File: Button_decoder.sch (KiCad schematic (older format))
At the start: 18 parts

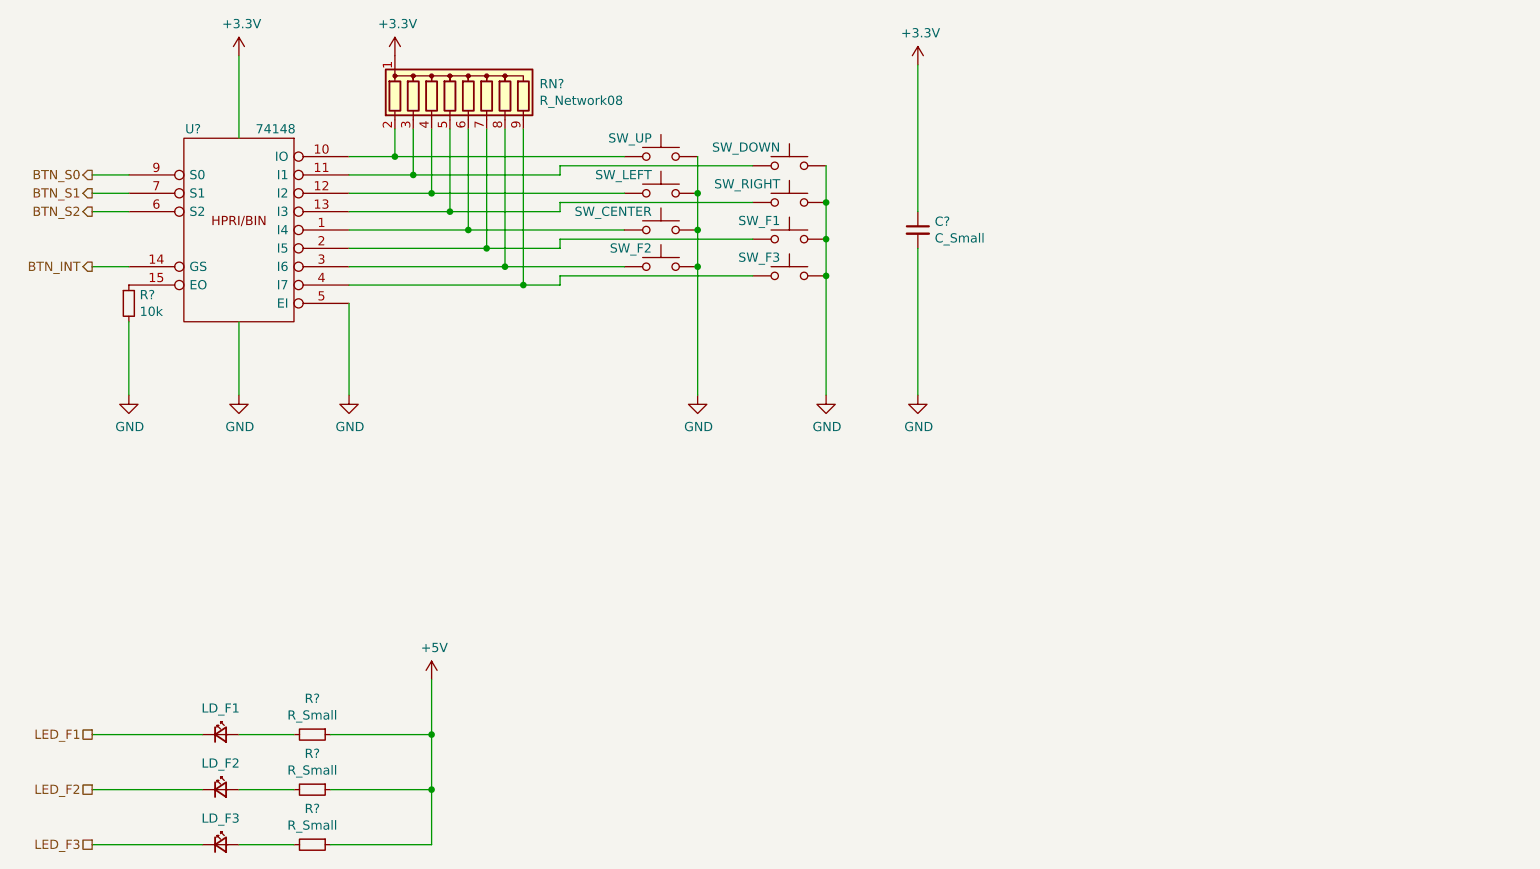
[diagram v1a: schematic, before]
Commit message: Bauteile grob platziert
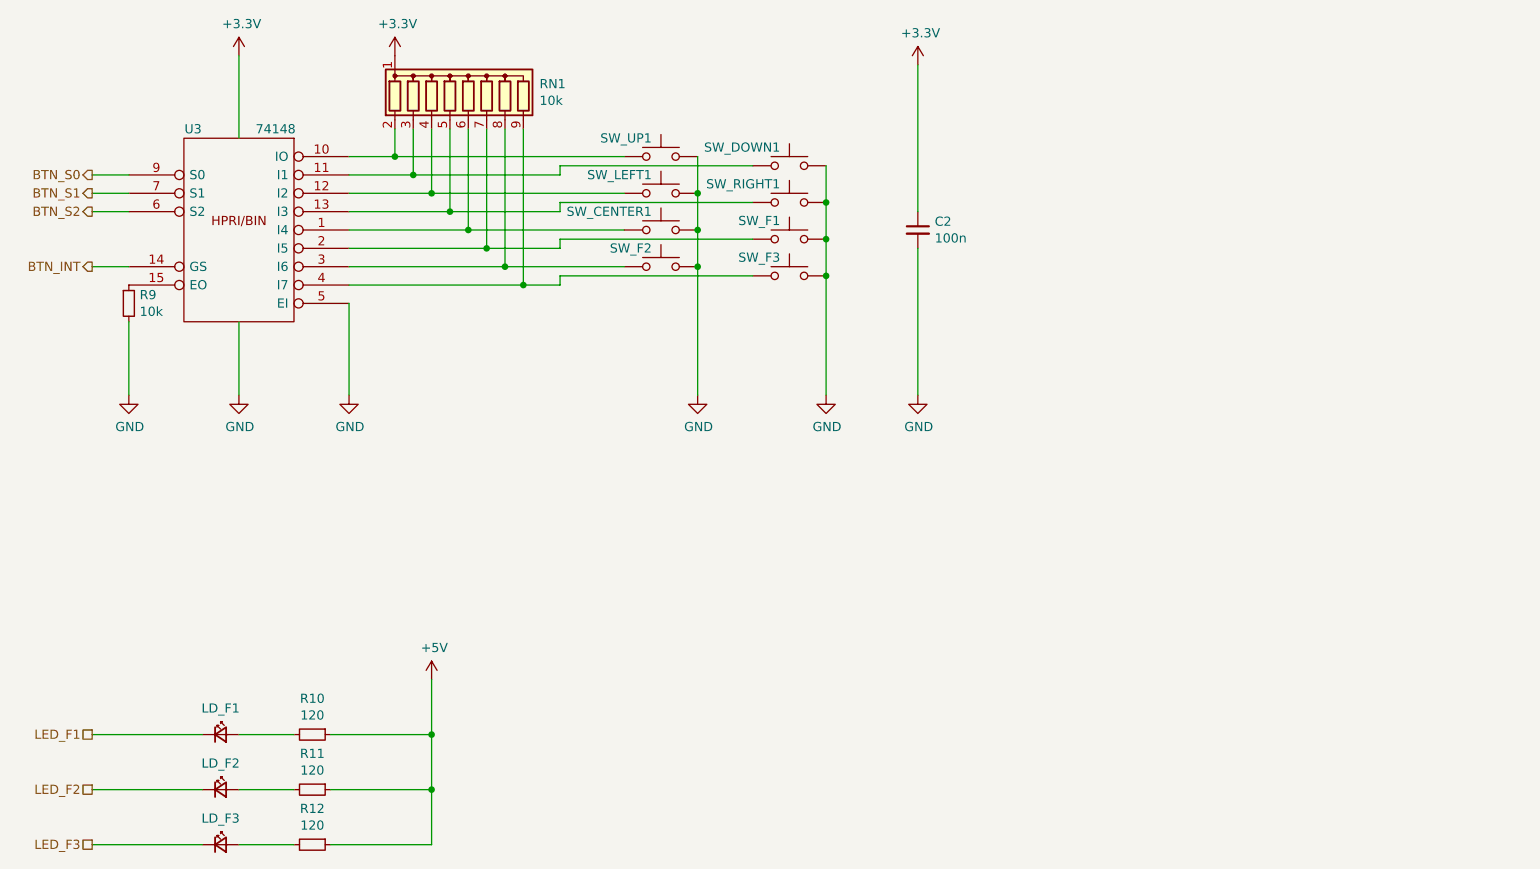
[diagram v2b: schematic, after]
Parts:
- C2: renamed from C?; value C_Small -> 100n; footprint (none) -> Capacitor_SMD:C_0603_1608Metric_Pad1.05x0.95mm_HandSolder
- LD_F1, LD_F2, LD_F3: footprint (none) -> LED_THT:LED_D3.0mm
- R10, R11, R12: renamed from R?; value R_Small -> 120; footprint (none) -> Resistor_SMD:R_0603_1608Metric_Pad1.05x0.95mm_HandSolder
- R9: renamed from R?; footprint (none) -> Resistor_SMD:R_0603_1608Metric_Pad1.05x0.95mm_HandSolder
- RN1: renamed from RN?; value R_Network08 -> 10k
- SW_CENTER1: renamed from SW_CENTER; footprint (none) -> Button_Switch_SMD:SW_MEC_5GSH9
- SW_DOWN1: renamed from SW_DOWN; footprint (none) -> Button_Switch_SMD:SW_MEC_5GSH9
- SW_F1, SW_F2, SW_F3: footprint (none) -> Button_Switch_SMD:SW_MEC_5GSH9
- SW_LEFT1: renamed from SW_LEFT; footprint (none) -> Button_Switch_SMD:SW_MEC_5GSH9
- SW_RIGHT1: renamed from SW_RIGHT; footprint (none) -> Button_Switch_SMD:SW_MEC_5GSH9
- SW_UP1: renamed from SW_UP; footprint (none) -> Button_Switch_SMD:SW_MEC_5GSH9
- U3: renamed from U?; footprint (none) -> Package_SO:SOIC-16_3.9x9.9mm_P1.27mm
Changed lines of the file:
@@
 BTN_INT
 $Comp
-L 74xx_IEEE:74148 U?
+L 74xx_IEEE:74148 U3
 U 1 1 5EFADAFE
 P 3300 2750
-F 0 "U?" H 3550 3300 50  0000 C CNN
+F 0 "U3" H 3550 3300 50  0000 C CNN
 F 1 "74148" H 3100 3300 50  0000 C CNN
-F 2 "" H 3300 2750 50  0001 C CNN
+F 2 "Package_SO:SOIC-16_3.9x9.9mm_P1.27mm" H 3300 2750 50  0001 C CNN
 F 3 "" H 3300 2750 50  0001 C CNN
 	1    3300 2750
@@
 	2500 2950 2700 2950
 $Comp
-L power:+3.3V #PWR?
+L power:+3.3V #PWR0110
 U 1 1 5EFAFAAB
 P 3300 1800
-F 0 "#PWR?" H 3300 1650 50  0001 C CNN
+F 0 "#PWR0110" H 3300 1650 50  0001 C CNN
 F 1 "+3.3V" H 3315 1973 50  0000 C CNN
 F 2 "" H 3300 1800 50  0001 C CNN
@@
 	3300 1800 3300 2250
 $Comp
-L power:GND #PWR?
+L power:GND #PWR0111
 U 1 1 5EFAFEDD
 P 3300 3650
-F 0 "#PWR?" H 3300 3400 50  0001 C CNN
+F 0 "#PWR0111" H 3300 3400 50  0001 C CNN
 F 1 "GND" H 3305 3477 50  0000 C CNN
 F 2 "" H 3300 3650 50  0001 C CNN
@@
 	3300 3650 3300 3250
 $Comp
-L power:GND #PWR?
+L power:GND #PWR0112
 U 1 1 5EFB0576
 P 2700 3650
-F 0 "#PWR?" H 2700 3400 50  0001 C CNN
+F 0 "#PWR0112" H 2700 3400 50  0001 C CNN
 F 1 "GND" H 2705 3477 50  0000 C CNN
 F 2 "" H 2700 3650 50  0001 C CNN
@@
 $EndComp
 $Comp
-L Device:R_Small R?
+L Device:R_Small R9
 U 1 1 5EFB06F4
 P 2700 3150
-F 0 "R?" H 2759 3196 50  0000 L CNN
+F 0 "R9" H 2759 3196 50  0000 L CNN
 F 1 "10k" H 2759 3105 50  0000 L CNN
-F 2 "" H 2700 3150 50  0001 C CNN
+F 2 "Resistor_SMD:R_0603_1608Metric_Pad1.05x0.95mm_HandSolder" H 2700 3150 50  0001 C CNN
 F 3 "~" H 2700 3150 50  0001 C CNN
 	1    2700 3150
@@
 	2700 3250 2700 3650
 $Comp
-L Device:R_Network08 RN?
+L Device:R_Network08 RN1
 U 1 1 5EFB12E3
 P 4550 2000
-F 0 "RN?" H 4938 2046 50  0000 L CNN
-F 1 "R_Network08" H 4938 1955 50  0000 L CNN
+F 0 "RN1" H 4938 2046 50  0000 L CNN
+F 1 "10k" H 4938 1955 50  0000 L CNN
 F 2 "Resistor_THT:R_Array_SIP9" V 5025 2000 50  0001 C CNN
 F 3 "http://www.vishay.com/docs/31509/csc.pdf" H 4550 2000 50  0001 C CNN
@@
 $EndComp
 $Comp
-L power:+3.3V #PWR?
+L power:+3.3V #PWR0113
 U 1 1 5EFB2E2E
 P 4150 1800
-F 0 "#PWR?" H 4150 1650 50  0001 C CNN
+F 0 "#PWR0113" H 4150 1650 50  0001 C CNN
 F 1 "+3.3V" H 4165 1973 50  0000 C CNN
 F 2 "" H 4150 1800 50  0001 C CNN
@@
 $EndComp
 $Comp
-L Switch:SW_MEC_5G SW_UP
+L Switch:SW_MEC_5G SW_UP1
 U 1 1 5EFB42CA
 P 5600 2350
-F 0 "SW_UP" H 5550 2450 50  0000 R CNN
+F 0 "SW_UP1" H 5550 2450 50  0000 R CNN
 F 1 "SW_MEC_5G" H 5850 2450 50  0001 C CNN
-F 2 "" H 5600 2550 50  0001 C CNN
+F 2 "Button_Switch_SMD:SW_MEC_5GSH9" H 5600 2550 50  0001 C CNN
 F 3 "http://www.apem.com/int/index.php?controller=attachment&id_attachment=488" H 5600 2550 50  0001 C CNN
 	1    5600 2350
@@
 	4850 3050 3900 3050
 $Comp
-L Switch:SW_MEC_5G SW_LEFT
+L Switch:SW_MEC_5G SW_LEFT1
 U 1 1 5EFE1803
 P 5600 2550
-F 0 "SW_LEFT" H 5550 2650 50  0000 R CNN
+F 0 "SW_LEFT1" H 5550 2650 50  0000 R CNN
 F 1 "SW_MEC_5G" H 5850 2650 50  0001 C CNN
-F 2 "" H 5600 2750 50  0001 C CNN
+F 2 "Button_Switch_SMD:SW_MEC_5GSH9" H 5600 2750 50  0001 C CNN
 F 3 "http://www.apem.com/int/index.php?controller=attachment&id_attachment=488" H 5600 2750 50  0001 C CNN
 	1    5600 2550
@@
 $EndComp
 $Comp
-L Switch:SW_MEC_5G SW_CENTER
+L Switch:SW_MEC_5G SW_CENTER1
 U 1 1 5EFE1FDD
 P 5600 2750
-F 0 "SW_CENTER" H 5550 2850 50  0000 R CNN
+F 0 "SW_CENTER1" H 5550 2850 50  0000 R CNN
 F 1 "SW_MEC_5G" H 5850 2850 50  0001 C CNN
-F 2 "" H 5600 2950 50  0001 C CNN
+F 2 "Button_Switch_SMD:SW_MEC_5GSH9" H 5600 2950 50  0001 C CNN
 F 3 "http://www.apem.com/int/index.php?controller=attachment&id_attachment=488" H 5600 2950 50  0001 C CNN
 	1    5600 2750
@@
 F 0 "SW_F2" H 5550 3050 50  0000 R CNN
 F 1 "SW_MEC_5G" H 5850 3050 50  0001 C CNN
-F 2 "" H 5600 3150 50  0001 C CNN
+F 2 "Button_Switch_SMD:SW_MEC_5GSH9" H 5600 3150 50  0001 C CNN
 F 3 "http://www.apem.com/int/index.php?controller=attachment&id_attachment=488" H 5600 3150 50  0001 C CNN
 	1    5600 2950
@@
 $EndComp
 $Comp
-L Switch:SW_MEC_5G SW_DOWN
+L Switch:SW_MEC_5G SW_DOWN1
 U 1 1 5EFF38EE
 P 6300 2400
-F 0 "SW_DOWN" H 6250 2500 50  0000 R CNN
+F 0 "SW_DOWN1" H 6250 2500 50  0000 R CNN
 F 1 "SW_MEC_5G" H 6550 2500 50  0001 C CNN
-F 2 "" H 6300 2600 50  0001 C CNN
+F 2 "Button_Switch_SMD:SW_MEC_5GSH9" H 6300 2600 50  0001 C CNN
 F 3 "http://www.apem.com/int/index.php?controller=attachment&id_attachment=488" H 6300 2600 50  0001 C CNN
 	1    6300 2400
@@
 $EndComp
 $Comp
-L Switch:SW_MEC_5G SW_RIGHT
+L Switch:SW_MEC_5G SW_RIGHT1
 U 1 1 5EFF3FB1
 P 6300 2600
-F 0 "SW_RIGHT" H 6250 2700 50  0000 R CNN
+F 0 "SW_RIGHT1" H 6250 2700 50  0000 R CNN
 F 1 "SW_MEC_5G" H 6550 2700 50  0001 C CNN
-F 2 "" H 6300 2800 50  0001 C CNN
+F 2 "Button_Switch_SMD:SW_MEC_5GSH9" H 6300 2800 50  0001 C CNN
 F 3 "http://www.apem.com/int/index.php?controller=attachment&id_attachment=488" H 6300 2800 50  0001 C CNN
 	1    6300 2600
@@
 F 0 "SW_F1" H 6250 2900 50  0000 R CNN
 F 1 "SW_MEC_5G" H 6550 2900 50  0001 C CNN
-F 2 "" H 6300 3000 50  0001 C CNN
+F 2 "Button_Switch_SMD:SW_MEC_5GSH9" H 6300 3000 50  0001 C CNN
 F 3 "http://www.apem.com/int/index.php?controller=attachment&id_attachment=488" H 6300 3000 50  0001 C CNN
 	1    6300 2800
@@
 F 0 "SW_F3" H 6250 3100 50  0000 R CNN
 F 1 "SW_MEC_5G" H 6550 3100 50  0001 C CNN
-F 2 "" H 6300 3200 50  0001 C CNN
+F 2 "Button_Switch_SMD:SW_MEC_5GSH9" H 6300 3200 50  0001 C CNN
 F 3 "http://www.apem.com/int/index.php?controller=attachment&id_attachment=488" H 6300 3200 50  0001 C CNN
 	1    6300 3000
@@
 $EndComp
 $Comp
-L power:GND #PWR?
+L power:GND #PWR0114
 U 1 1 5F000955
 P 5800 3650
-F 0 "#PWR?" H 5800 3400 50  0001 C CNN
+F 0 "#PWR0114" H 5800 3400 50  0001 C CNN
 F 1 "GND" H 5805 3477 50  0000 C CNN
 F 2 "" H 5800 3650 50  0001 C CNN
@@
 $EndComp
 $Comp
-L power:GND #PWR?
+L power:GND #PWR0115
 U 1 1 5F00123E
 P 6500 3650
-F 0 "#PWR?" H 6500 3400 50  0001 C CNN
+F 0 "#PWR0115" H 6500 3400 50  0001 C CNN
 F 1 "GND" H 6505 3477 50  0000 C CNN
 F 2 "" H 6500 3650 50  0001 C CNN
@@
 	6500 3000 6500 3650
 $Comp
-L power:GND #PWR?
+L power:GND #PWR0116
 U 1 1 5F008E80
 P 3900 3650
-F 0 "#PWR?" H 3900 3400 50  0001 C CNN
+F 0 "#PWR0116" H 3900 3400 50  0001 C CNN
 F 1 "GND" H 3905 3477 50  0000 C CNN
 F 2 "" H 3900 3650 50  0001 C CNN
@@
 	3900 3650 3900 3150
 $Comp
-L power:GND #PWR?
+L power:GND #PWR0117
 U 1 1 5F00A4A8
 P 7000 3650
-F 0 "#PWR?" H 7000 3400 50  0001 C CNN
+F 0 "#PWR0117" H 7000 3400 50  0001 C CNN
 F 1 "GND" H 7005 3477 50  0000 C CNN
 F 2 "" H 7000 3650 50  0001 C CNN
@@
 $EndComp
 $Comp
-L power:+3.3V #PWR?
+L power:+3.3V #PWR0118
 U 1 1 5F00BBF0
 P 7000 1850
-F 0 "#PWR?" H 7000 1700 50  0001 C CNN
+F 0 "#PWR0118" H 7000 1700 50  0001 C CNN
 F 1 "+3.3V" H 7015 2023 50  0000 C CNN
 F 2 "" H 7000 1850 50  0001 C CNN
@@
 $EndComp
 $Comp
-L Device:C_Small C?
+L Device:C_Small C2
 U 1 1 5F00C881
 P 7000 2750
-F 0 "C?" H 7092 2796 50  0000 L CNN
-F 1 "C_Small" H 7092 2705 50  0000 L CNN
-F 2 "" H 7000 2750 50  0001 C CNN
+F 0 "C2" H 7092 2796 50  0000 L CNN
+F 1 "100n" H 7092 2705 50  0000 L CNN
+F 2 "Capacitor_SMD:C_0603_1608Metric_Pad1.05x0.95mm_HandSolder" H 7000 2750 50  0001 C CNN
 F 3 "~" H 7000 2750 50  0001 C CNN
 	1    7000 2750
@@
 	7000 2850 7000 3650
 $Comp
-L Device:R_Small R?
+L Device:R_Small R10
 U 1 1 5F00F388
 P 3700 5500
-F 0 "R?" V 3504 5500 50  0000 C CNN
-F 1 "R_Small" V 3595 5500 50  0000 C CNN
-F 2 "" H 3700 5500 50  0001 C CNN
+F 0 "R10" V 3504 5500 50  0000 C CNN
+F 1 "120" V 3595 5500 50  0000 C CNN
+F 2 "Resistor_SMD:R_0603_1608Metric_Pad1.05x0.95mm_HandSolder" H 3700 5500 50  0001 C CNN
 F 3 "~" H 3700 5500 50  0001 C CNN
 	1    3700 5500
@@
 F 0 "LD_F1" H 3200 5643 50  0000 C CNN
 F 1 "LED_Small" H 3200 5644 50  0001 C CNN
-F 2 "" V 3200 5500 50  0001 C CNN
+F 2 "LED_THT:LED_D3.0mm" V 3200 5500 50  0001 C CNN
 F 3 "~" V 3200 5500 50  0001 C CNN
 	1    3200 5500
@@
 	3300 5500 3600 5500
 $Comp
-L Device:R_Small R?
+L Device:R_Small R11
 U 1 1 5F011E08
 P 3700 5800
-F 0 "R?" V 3504 5800 50  0000 C CNN
-F 1 "R_Small" V 3595 5800 50  0000 C CNN
-F 2 "" H 3700 5800 50  0001 C CNN
+F 0 "R11" V 3504 5800 50  0000 C CNN
+F 1 "120" V 3595 5800 50  0000 C CNN
+F 2 "Resistor_SMD:R_0603_1608Metric_Pad1.05x0.95mm_HandSolder" H 3700 5800 50  0001 C CNN
 F 3 "~" H 3700 5800 50  0001 C CNN
 	1    3700 5800
@@
 F 0 "LD_F2" H 3200 5943 50  0000 C CNN
 F 1 "LED_Small" H 3200 5944 50  0001 C CNN
-F 2 "" V 3200 5800 50  0001 C CNN
+F 2 "LED_THT:LED_D3.0mm" V 3200 5800 50  0001 C CNN
 F 3 "~" V 3200 5800 50  0001 C CNN
 	1    3200 5800
@@
 	3300 5800 3600 5800
 $Comp
-L Device:R_Small R?
+L Device:R_Small R12
 U 1 1 5F01298E
 P 3700 6100
-F 0 "R?" V 3504 6100 50  0000 C CNN
-F 1 "R_Small" V 3595 6100 50  0000 C CNN
-F 2 "" H 3700 6100 50  0001 C CNN
+F 0 "R12" V 3504 6100 50  0000 C CNN
+F 1 "120" V 3595 6100 50  0000 C CNN
+F 2 "Resistor_SMD:R_0603_1608Metric_Pad1.05x0.95mm_HandSolder" H 3700 6100 50  0001 C CNN
 F 3 "~" H 3700 6100 50  0001 C CNN
 	1    3700 6100
@@
 F 0 "LD_F3" H 3200 6243 50  0000 C CNN
 F 1 "LED_Small" H 3200 6244 50  0001 C CNN
-F 2 "" V 3200 6100 50  0001 C CNN
+F 2 "LED_THT:LED_D3.0mm" V 3200 6100 50  0001 C CNN
 F 3 "~" V 3200 6100 50  0001 C CNN
 	1    3200 6100
@@
 	3300 6100 3600 6100
 $Comp
-L power:+5V #PWR?
+L power:+5V #PWR0119
 U 1 1 5F01432E
 P 4350 5200
-F 0 "#PWR?" H 4350 5050 50  0001 C CNN
+F 0 "#PWR0119" H 4350 5050 50  0001 C CNN
 F 1 "+5V" H 4365 5373 50  0000 C CNN
 F 2 "" H 4350 5200 50  0001 C CNN

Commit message: Alle Bauteile platziert
Alle Bauteile sind grob plaziert.
Einige Bauteile sollten noch umplaziert werden (u. a. die Jumper links neben Groov-Con, RGB-LED,).
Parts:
- C2: symbol Device:C_Small -> MCT_Labor_5529-rescue:C_Small-Device
- LD_F1, LD_F2, LD_F3: symbol Device:LED_Small -> MCT_Labor_5529-rescue:LED_Small-Device
- R10, R11, R12, R9: symbol Device:R_Small -> MCT_Labor_5529-rescue:R_Small-Device
- RN1: symbol Device:R_Network08 -> MCT_Labor_5529-rescue:R_Network08-Device
- SW_CENTER1, SW_DOWN1, SW_F1, SW_F2, SW_F3, SW_LEFT1, SW_RIGHT1, SW_UP1: symbol Switch:SW_MEC_5G -> MCT_Labor_5529-rescue:SW_MEC_5G-Switch
- U3: symbol 74xx_IEEE:74148 -> MCT_Labor_5529-rescue:74148-74xx_IEEE
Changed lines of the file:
@@
 BTN_INT
 $Comp
-L 74xx_IEEE:74148 U3
+L MCT_Labor_5529-rescue:74148-74xx_IEEE U3
 U 1 1 5EFADAFE
 P 3300 2750
@@
 	2500 2950 2700 2950
 $Comp
-L power:+3.3V #PWR0110
+L MCT_Labor_5529-rescue:+3.3V-power #PWR0110
 U 1 1 5EFAFAAB
 P 3300 1800
@@
 	3300 1800 3300 2250
 $Comp
-L power:GND #PWR0111
+L MCT_Labor_5529-rescue:GND-power #PWR0111
 U 1 1 5EFAFEDD
 P 3300 3650
@@
 	3300 3650 3300 3250
 $Comp
-L power:GND #PWR0112
+L MCT_Labor_5529-rescue:GND-power #PWR0112
 U 1 1 5EFB0576
 P 2700 3650
@@
 $EndComp
 $Comp
-L Device:R_Small R9
+L MCT_Labor_5529-rescue:R_Small-Device R9
 U 1 1 5EFB06F4
 P 2700 3150
@@
 	2700 3250 2700 3650
 $Comp
-L Device:R_Network08 RN1
+L MCT_Labor_5529-rescue:R_Network08-Device RN1
 U 1 1 5EFB12E3
 P 4550 2000
@@
 $EndComp
 $Comp
-L power:+3.3V #PWR0113
+L MCT_Labor_5529-rescue:+3.3V-power #PWR0113
 U 1 1 5EFB2E2E
 P 4150 1800
@@
 $EndComp
 $Comp
-L Switch:SW_MEC_5G SW_UP1
+L MCT_Labor_5529-rescue:SW_MEC_5G-Switch SW_UP1
 U 1 1 5EFB42CA
 P 5600 2350
@@
 	4850 3050 3900 3050
 $Comp
-L Switch:SW_MEC_5G SW_LEFT1
+L MCT_Labor_5529-rescue:SW_MEC_5G-Switch SW_LEFT1
 U 1 1 5EFE1803
 P 5600 2550
@@
 $EndComp
 $Comp
-L Switch:SW_MEC_5G SW_CENTER1
+L MCT_Labor_5529-rescue:SW_MEC_5G-Switch SW_CENTER1
 U 1 1 5EFE1FDD
 P 5600 2750
@@
 $EndComp
 $Comp
-L Switch:SW_MEC_5G SW_F2
+L MCT_Labor_5529-rescue:SW_MEC_5G-Switch SW_F2
 U 1 1 5EFE26F5
 P 5600 2950
@@
 $EndComp
 $Comp
-L Switch:SW_MEC_5G SW_DOWN1
+L MCT_Labor_5529-rescue:SW_MEC_5G-Switch SW_DOWN1
 U 1 1 5EFF38EE
 P 6300 2400
@@
 $EndComp
 $Comp
-L Switch:SW_MEC_5G SW_RIGHT1
+L MCT_Labor_5529-rescue:SW_MEC_5G-Switch SW_RIGHT1
 U 1 1 5EFF3FB1
 P 6300 2600
@@
 $EndComp
 $Comp
-L Switch:SW_MEC_5G SW_F1
+L MCT_Labor_5529-rescue:SW_MEC_5G-Switch SW_F1
 U 1 1 5EFF483B
 P 6300 2800
@@
 $EndComp
 $Comp
-L Switch:SW_MEC_5G SW_F3
+L MCT_Labor_5529-rescue:SW_MEC_5G-Switch SW_F3
 U 1 1 5EFF4FB0
 P 6300 3000
@@
 $EndComp
 $Comp
-L power:GND #PWR0114
+L MCT_Labor_5529-rescue:GND-power #PWR0114
 U 1 1 5F000955
 P 5800 3650
@@
 $EndComp
 $Comp
-L power:GND #PWR0115
+L MCT_Labor_5529-rescue:GND-power #PWR0115
 U 1 1 5F00123E
 P 6500 3650
@@
 	6500 3000 6500 3650
 $Comp
-L power:GND #PWR0116
+L MCT_Labor_5529-rescue:GND-power #PWR0116
 U 1 1 5F008E80
 P 3900 3650
@@
 	3900 3650 3900 3150
 $Comp
-L power:GND #PWR0117
+L MCT_Labor_5529-rescue:GND-power #PWR0117
 U 1 1 5F00A4A8
 P 7000 3650
@@
 $EndComp
 $Comp
-L power:+3.3V #PWR0118
+L MCT_Labor_5529-rescue:+3.3V-power #PWR0118
 U 1 1 5F00BBF0
 P 7000 1850
@@
 $EndComp
 $Comp
-L Device:C_Small C2
+L MCT_Labor_5529-rescue:C_Small-Device C2
 U 1 1 5F00C881
 P 7000 2750
@@
 	7000 2850 7000 3650
 $Comp
-L Device:R_Small R10
+L MCT_Labor_5529-rescue:R_Small-Device R10
 U 1 1 5F00F388
 P 3700 5500
@@
 $EndComp
 $Comp
-L Device:LED_Small LD_F1
+L MCT_Labor_5529-rescue:LED_Small-Device LD_F1
 U 1 1 5F00FA81
 P 3200 5500
@@
 	3300 5500 3600 5500
 $Comp
-L Device:R_Small R11
+L MCT_Labor_5529-rescue:R_Small-Device R11
 U 1 1 5F011E08
 P 3700 5800
@@
 $EndComp
 $Comp
-L Device:LED_Small LD_F2
+L MCT_Labor_5529-rescue:LED_Small-Device LD_F2
 U 1 1 5F011E0E
 P 3200 5800
@@
 	3300 5800 3600 5800
 $Comp
-L Device:R_Small R12
+L MCT_Labor_5529-rescue:R_Small-Device R12
 U 1 1 5F01298E
 P 3700 6100
@@
 $EndComp
 $Comp
-L Device:LED_Small LD_F3
+L MCT_Labor_5529-rescue:LED_Small-Device LD_F3
 U 1 1 5F012994
 P 3200 6100
@@
 	3300 6100 3600 6100
 $Comp
-L power:+5V #PWR0119
+L MCT_Labor_5529-rescue:+5V-power #PWR0119
 U 1 1 5F01432E
 P 4350 5200

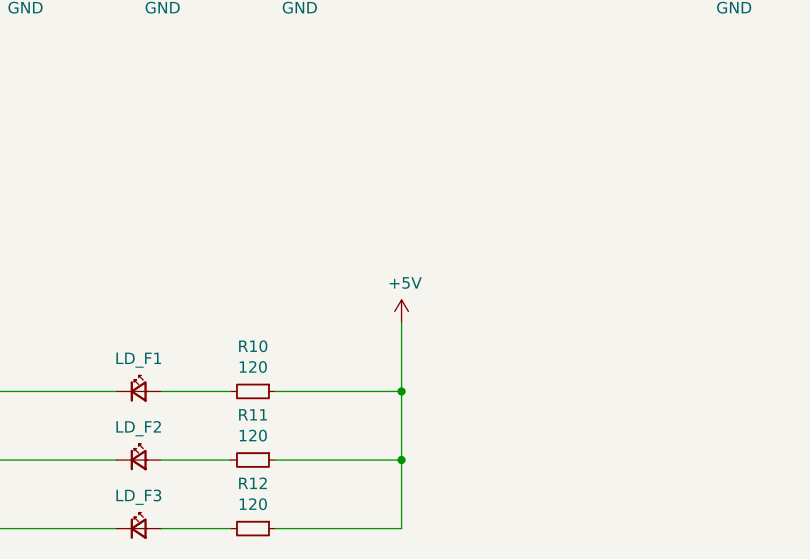
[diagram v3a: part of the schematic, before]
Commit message: Anpassungen am Lüfteranschluss und den LEDs
-Lüfteranschluss verändert
 -> 12V-Versorgung eingefügt
-LED & LCD auf 3,3V umgestellt
 -> Ladungspunpe für neg. Kontrastspannung
-keine 5V Versorgung mehr
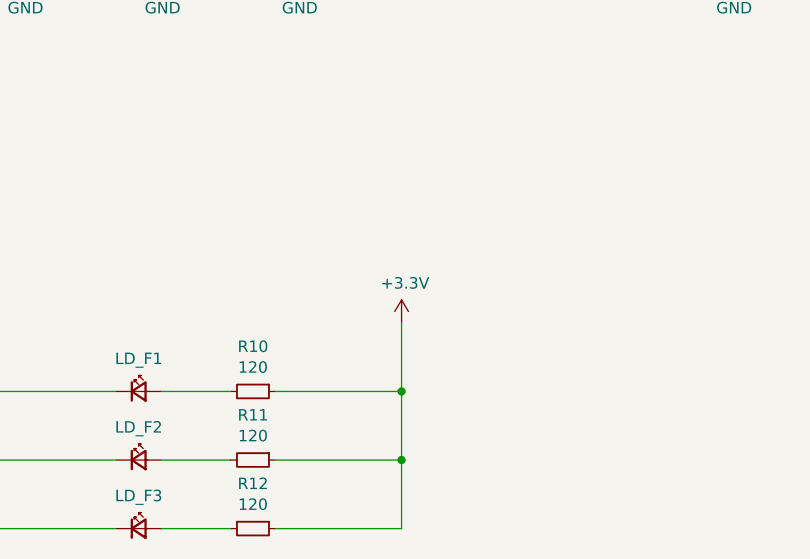
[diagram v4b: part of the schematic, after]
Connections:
- net +5V is gone; now on net +3V3: R10.1, R11.1, R12.1
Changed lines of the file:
@@
 Wire Wire Line
 	3300 6100 3600 6100
-$Comp
-L MCT_Labor_5529-rescue:+5V-power #PWR0119
-U 1 1 5F01432E
-P 4350 5200
-F 0 "#PWR0119" H 4350 5050 50  0001 C CNN
-F 1 "+5V" H 4365 5373 50  0000 C CNN
-F 2 "" H 4350 5200 50  0001 C CNN
-F 3 "" H 4350 5200 50  0001 C CNN
-	1    4350 5200
-	1    0    0    -1
-$EndComp
 Wire Wire Line
 	4350 5200 4350 5500
@@
 Wire Wire Line
 	2500 5500 3100 5500
+$Comp
+L power:+3.3V #PWR016
+U 1 1 5F31A2F8
+P 4350 5200
+F 0 "#PWR016" H 4350 5050 50  0001 C CNN
+F 1 "+3.3V" H 4365 5373 50  0000 C CNN
+F 2 "" H 4350 5200 50  0001 C CNN
+F 3 "" H 4350 5200 50  0001 C CNN
+	1    4350 5200
+	1    0    0    -1
+$EndComp
 $EndSCHEMATC
